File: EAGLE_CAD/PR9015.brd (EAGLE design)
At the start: 70 x 70 mm, 73 parts, among them J1 M3_SCREW_POST, SW1 C&K_PTS645

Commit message: Revert cea9e40..4e97d22
This rolls back to commit cea9e40d509ff5bb8dd7e4369702d55ec1f1bc0f.
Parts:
- C17: device PR_Parts_Library:C0402 -> resistor:C0402
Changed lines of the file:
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@@
 <?xml version="1.0" encoding="utf-8"?>
 <!DOCTYPE eagle SYSTEM "eagle.dtd">
-<eagle version="6.6.0">
+<eagle version="7.2.0">
 <drawing>
 <settings>
@@
 <setting verticaltext="up"/>
 </settings>
-<grid distance="0.1" unitdist="mm" unit="mm" style="lines" multiple="1" display="yes" altdistance="0.025" altunitdist="inch" altunit="inch"/>
+<grid distance="1" unitdist="mil" unit="mm" style="lines" multiple="1" display="yes" altdistance="0.025" altunitdist="inch" altunit="inch"/>
 <layers>
 <layer number="1" name="Top" color="4" fill="1" visible="yes" active="yes"/>
@@
 <pass name="Default">
 <param name="RoutingGrid" value="50mil"/>
+<param name="AutoGrid" value="1"/>
+<param name="Efforts" value="0"/>
+<param name="TopRouterVariant" value="1"/>
 <param name="tpViaShape" value="round"/>
 <param name="PrefDir.1" value="|"/>
@@
 <attribute name="VALUE" x="32.235" y="7.905" size="1.27" layer="27" rot="R180"/>
 </element>
-<element name="C17" library="PR_Parts_Library" package="C0402" value="1uf" x="38.8" y="12.7" smashed="yes" rot="R180">
+<element name="C17" library="resistor" package="C0402" value="1uf" x="38.8" y="12.7" smashed="yes" rot="R180">
 <attribute name="NAME" x="40.265" y="12.535" size="0.6096" layer="25" ratio="16"/>
 <attribute name="VALUE" x="39.435" y="14.605" size="1.27" layer="27" rot="R180"/>
@@
 <wire x1="34.9" y1="12.4" x2="33.7" y2="12.4" width="0.4064" layer="16"/>
 <wire x1="33.7" y1="12.4" x2="31.3" y2="10" width="0.4064" layer="16"/>
-<wire x1="38.2929" y1="12.7" x2="37.85" y2="12.4" width="0.4064" layer="1"/>
+<wire x1="38.15" y1="12.7" x2="37.85" y2="12.4" width="0.4064" layer="1"/>
 <wire x1="37.85" y1="12.4" x2="36.9" y2="12.4" width="0.4064" layer="1"/>
 <via x="36.9" y="12.4" extent="1-16" drill="0.6"/>
 <wire x1="36.9" y1="12.4" x2="34.9" y2="12.4" width="0.4064" layer="16"/>
 <wire x1="38.15" y1="9.8" x2="38.15" y2="11.5" width="0.4064" layer="1"/>
-<wire x1="38.15" y1="11.5" x2="38.2929" y2="12.7" width="0.4064" layer="1"/>
+<wire x1="38.15" y1="11.5" x2="38.15" y2="12.7" width="0.4064" layer="1"/>
 <wire x1="31.3" y1="10" x2="31.3" y2="9.3" width="0.4064" layer="16"/>
 <via x="31.3" y="9.3" extent="1-16" drill="0.6" diameter="0.4064"/>
@@
 <wire x1="31.3" y1="9.3" x2="29.95" y2="9.3" width="0.4064" layer="1"/>
 <wire x1="29.95" y1="9.3" x2="29.9" y2="9.25" width="0.4064" layer="1"/>
-<wire x1="38.2929" y1="12.7" x2="38.15" y2="14" width="0.6096" layer="1"/>
+<wire x1="38.15" y1="12.7" x2="38.15" y2="14" width="0.6096" layer="1"/>
 </signal>
 <signal name="N$20">

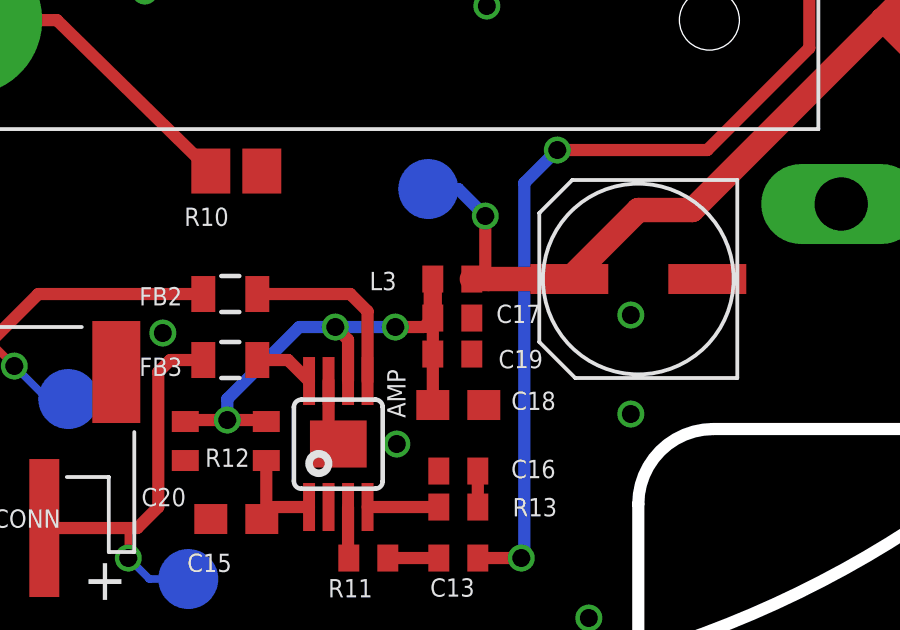
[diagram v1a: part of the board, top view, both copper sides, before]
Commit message: okay, now we're good i think
copied R_US over to PR_Parts_Library. Then added a new package variant
and connected it with my c0402 package (created from Chris’s email).
Then went into the .brd and replaced C17 with my new part. Seems to
work.
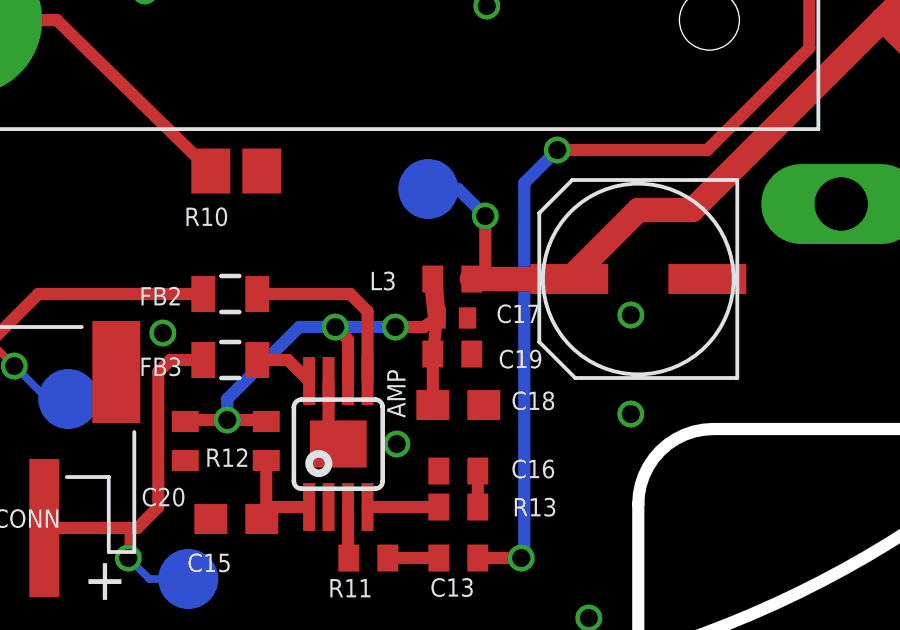
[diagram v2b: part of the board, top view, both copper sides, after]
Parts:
- C17: device resistor:C0402 -> PR_Parts_Library:C0402
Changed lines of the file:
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@@
 <?xml version="1.0" encoding="utf-8"?>
 <!DOCTYPE eagle SYSTEM "eagle.dtd">
-<eagle version="7.2.0">
+<eagle version="6.6.0">
 <drawing>
 <settings>
@@
 <setting verticaltext="up"/>
 </settings>
-<grid distance="1" unitdist="mil" unit="mm" style="lines" multiple="1" display="yes" altdistance="0.025" altunitdist="inch" altunit="inch"/>
+<grid distance="0.1" unitdist="mm" unit="mm" style="lines" multiple="1" display="yes" altdistance="0.025" altunitdist="inch" altunit="inch"/>
 <layers>
 <layer number="1" name="Top" color="4" fill="1" visible="yes" active="yes"/>
@@
 <pass name="Default">
 <param name="RoutingGrid" value="50mil"/>
-<param name="AutoGrid" value="1"/>
-<param name="Efforts" value="0"/>
-<param name="TopRouterVariant" value="1"/>
 <param name="tpViaShape" value="round"/>
 <param name="PrefDir.1" value="|"/>
@@
 <attribute name="VALUE" x="32.235" y="7.905" size="1.27" layer="27" rot="R180"/>
 </element>
-<element name="C17" library="resistor" package="C0402" value="1uf" x="38.8" y="12.7" smashed="yes" rot="R180">
+<element name="C17" library="PR_Parts_Library" package="C0402" value="1uf" x="38.8" y="12.7" smashed="yes" rot="R180">
 <attribute name="NAME" x="40.265" y="12.535" size="0.6096" layer="25" ratio="16"/>
 <attribute name="VALUE" x="39.435" y="14.605" size="1.27" layer="27" rot="R180"/>
@@
 <wire x1="34.9" y1="12.4" x2="33.7" y2="12.4" width="0.4064" layer="16"/>
 <wire x1="33.7" y1="12.4" x2="31.3" y2="10" width="0.4064" layer="16"/>
-<wire x1="38.15" y1="12.7" x2="37.85" y2="12.4" width="0.4064" layer="1"/>
+<wire x1="38.2929" y1="12.7" x2="37.85" y2="12.4" width="0.4064" layer="1"/>
 <wire x1="37.85" y1="12.4" x2="36.9" y2="12.4" width="0.4064" layer="1"/>
 <via x="36.9" y="12.4" extent="1-16" drill="0.6"/>
 <wire x1="36.9" y1="12.4" x2="34.9" y2="12.4" width="0.4064" layer="16"/>
 <wire x1="38.15" y1="9.8" x2="38.15" y2="11.5" width="0.4064" layer="1"/>
-<wire x1="38.15" y1="11.5" x2="38.15" y2="12.7" width="0.4064" layer="1"/>
+<wire x1="38.15" y1="11.5" x2="38.2929" y2="12.7" width="0.4064" layer="1"/>
 <wire x1="31.3" y1="10" x2="31.3" y2="9.3" width="0.4064" layer="16"/>
 <via x="31.3" y="9.3" extent="1-16" drill="0.6" diameter="0.4064"/>
@@
 <wire x1="31.3" y1="9.3" x2="29.95" y2="9.3" width="0.4064" layer="1"/>
 <wire x1="29.95" y1="9.3" x2="29.9" y2="9.25" width="0.4064" layer="1"/>
-<wire x1="38.15" y1="12.7" x2="38.15" y2="14" width="0.6096" layer="1"/>
+<wire x1="38.2929" y1="12.7" x2="38.15" y2="14" width="0.6096" layer="1"/>
 </signal>
 <signal name="N$20">
